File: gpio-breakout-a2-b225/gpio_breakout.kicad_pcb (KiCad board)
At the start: 4 copper layers, 63.5 x 32 mm, 9 parts, among them J1 ZF5S-40-01-T-WT-K-TR, J2 Pi GPIO 2x20

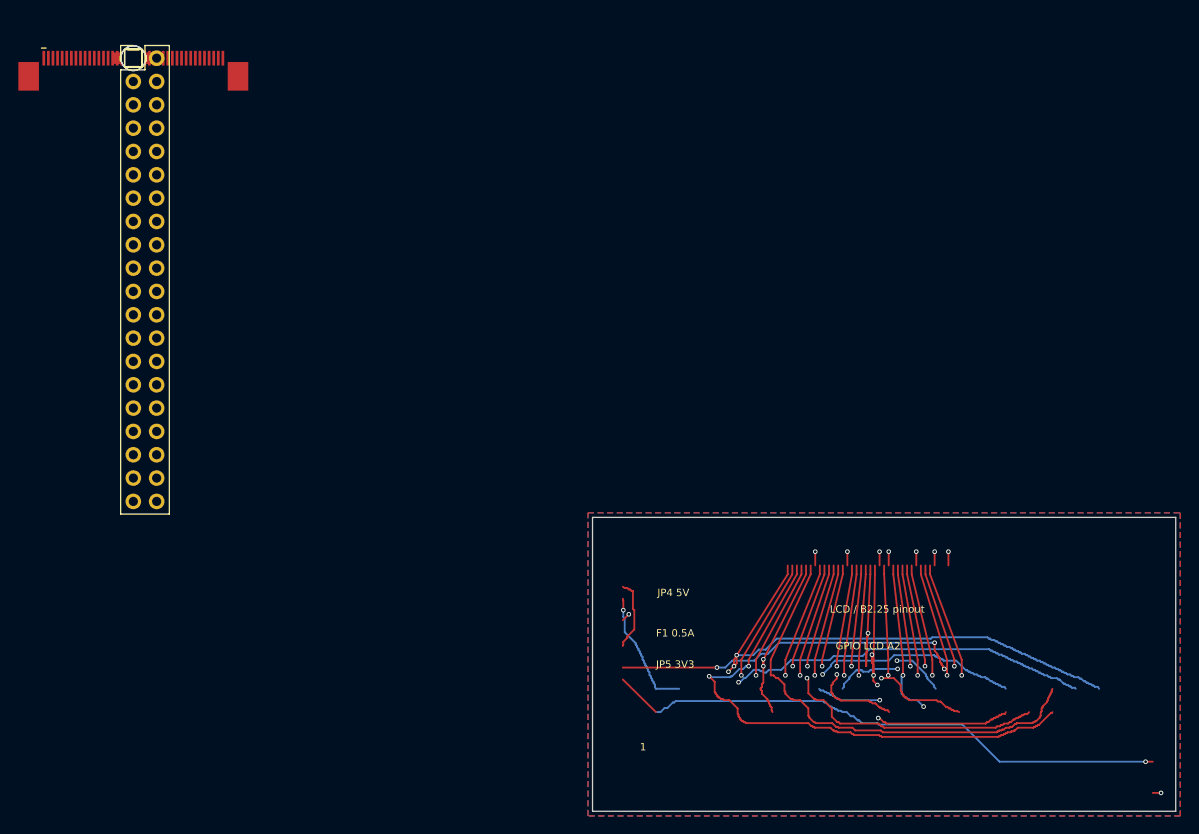
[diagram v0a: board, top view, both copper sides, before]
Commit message: Add protected USB2 input to B2.25 GPIO LCD addon
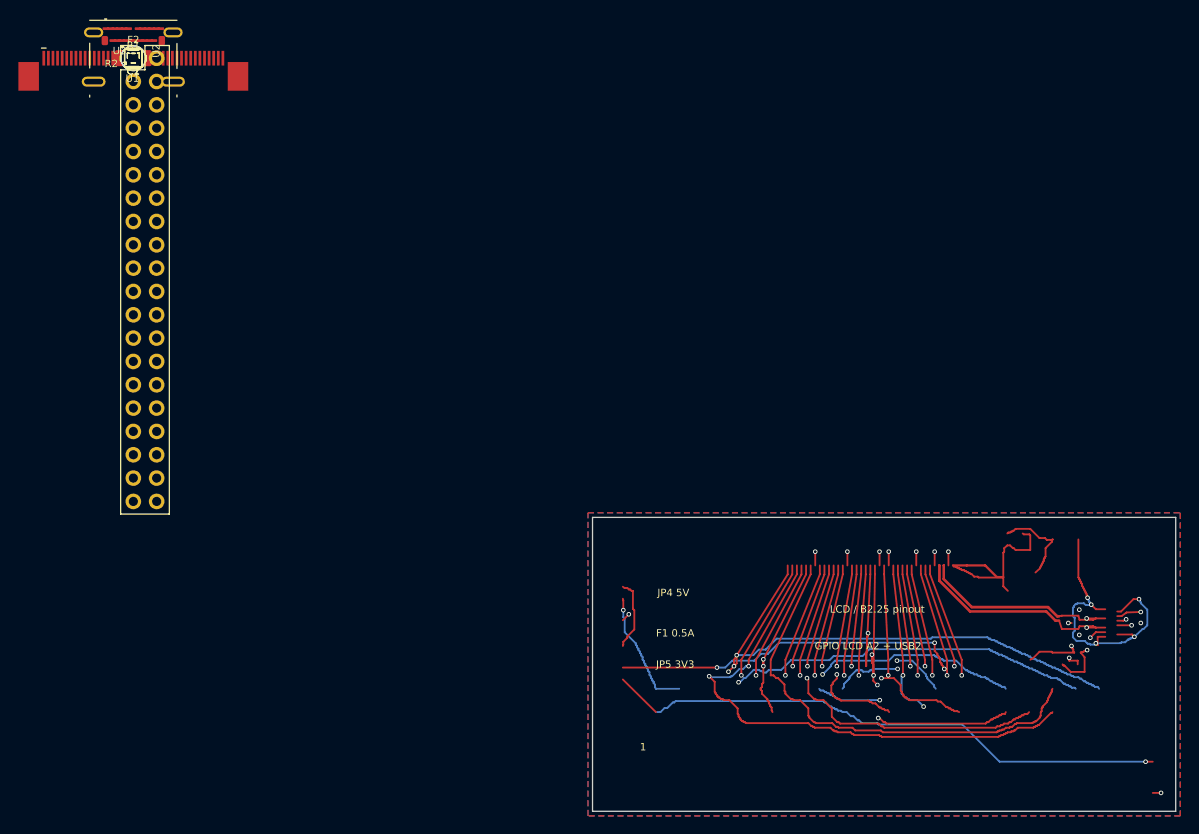
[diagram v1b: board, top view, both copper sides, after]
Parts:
- added C1: 1u 16V X7R, Capacitor_SMD:C_0603_1608Metric, F.Cu at (0.00, 0.00)
- added C2: 100n 16V X7R, Capacitor_SMD:C_0603_1608Metric, F.Cu at (0.00, 0.00)
- added F2: SMD1206P050TF/15, Fuse:Fuse_1206_3216Metric, F.Cu at (0.00, 0.00)
- added J3: 1054500101, USB_A2:USB_C_Receptacle_Molex_105450-0101, F.Cu at (0.00, 0.00)
- added R1, R2: 5.1k 1%, Resistor_SMD:R_0603_1608Metric, F.Cu at (0.00, 0.00)
- added U1: LM66100DCKR, Package_TO_SOT_SMD:SOT-363_SC-70-6, F.Cu at (0.00, 0.00)
- added U2, U3: TPD2EUSB30DRTR, Package_TO_SOT_SMD:Texas_DRT-3, F.Cu at (0.00, 0.00)
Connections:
- J1 pad 1: (no net) -> USB_VBUS
- J1 pad 2: (no net) -> USB_VBUS
- J1 pad 3: (no net) -> USB_VBUS
- J1 pad 4: (no net) -> USB_VBUS
- J1 pad 6: (no net) -> USB_D_N
- J1 pad 7: (no net) -> USB_D_P
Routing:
- net USB_D_N: track 0.00 -> 45.2 mm, vias 0 -> 2
- net USB_D_P: track 0.00 -> 35.5 mm, vias 0 -> 2
- net USB_VBUS_RAW: track 0.00 -> 34.7 mm, vias 0 -> 5
- net USB_VBUS: track 0.00 -> 22.6 mm
- net USB_CC2: track 0.00 -> 17.8 mm, vias 0 -> 2
- net USB_CC1: track 0.00 -> 10.3 mm, vias 0 -> 2
- net USB_VBUS_IN: track 0.00 -> 10.0 mm
- net GND: track 11.4 -> 13.4 mm, vias 8 -> 13
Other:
- board text added: "GPIO LCD A2 + USB2"
- board text added: "USB HOST INPUT / LCD POWER LINKS OPEN"
- board text removed: "GPIO LCD A2"
- board text removed: "USB pins 1-4,6,7 not connected"
